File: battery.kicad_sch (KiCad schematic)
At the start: 25 parts

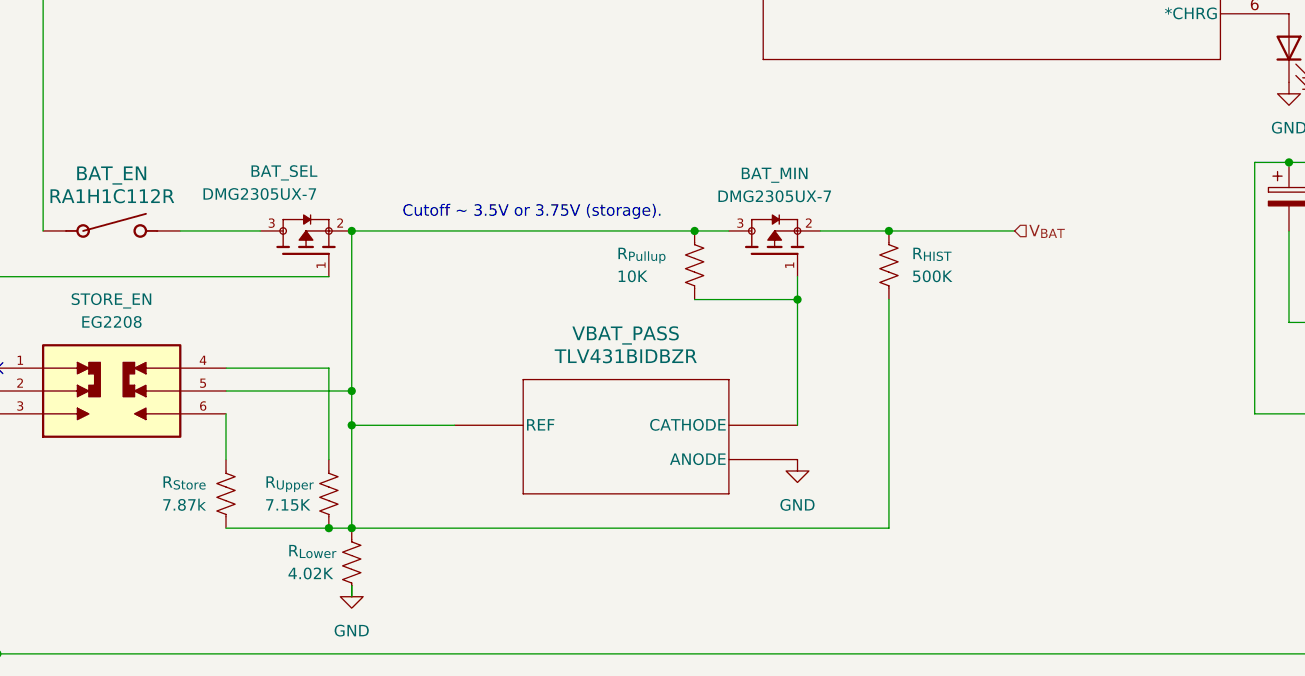
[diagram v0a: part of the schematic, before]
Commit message: Adjust battery resistor values
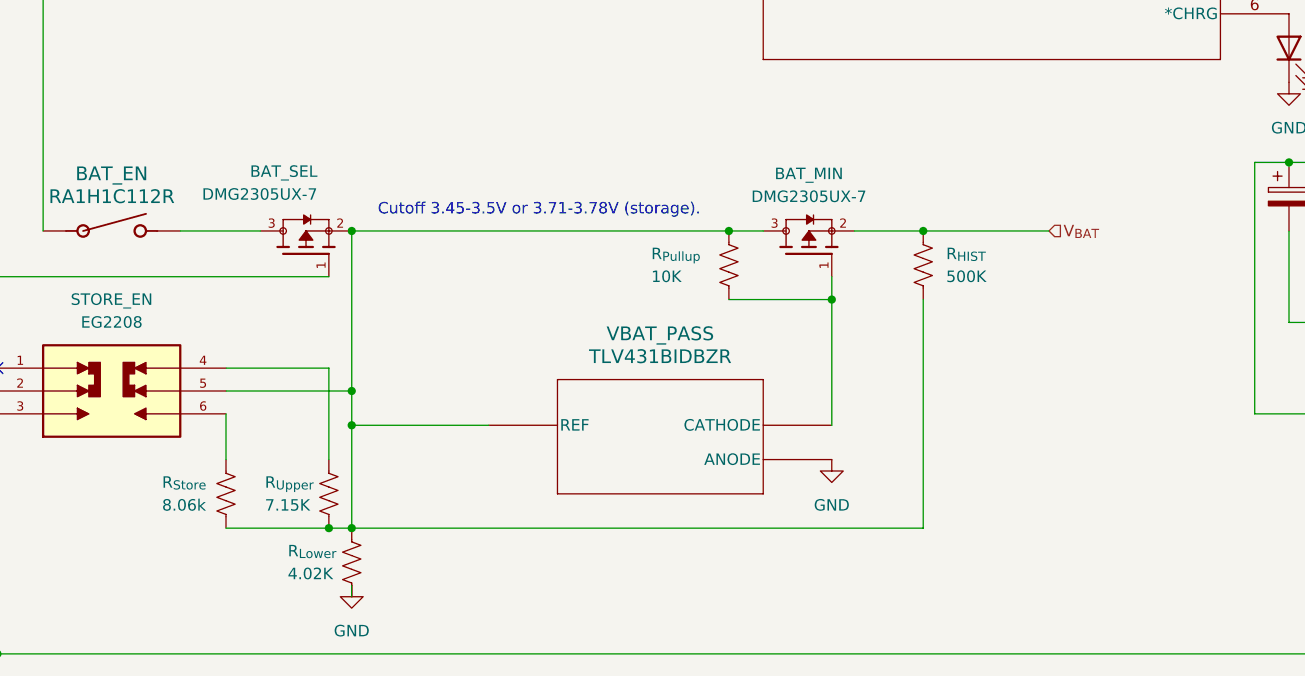
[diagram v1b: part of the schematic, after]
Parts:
- R_{Store}: value 7.87k -> 8.06k
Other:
- note added: "Cutoff 3.45-3.5V or 3.71-3.78V (storage)."
- note removed: "Cutoff ~ 3.5V or 3.75V (storage)."
- moved on the sheet: BAT_MIN, R_{HIST}, R_{Pullup}, VBAT_PASS
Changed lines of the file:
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@@
 		)
 	)
-	(text "Cutoff ~ 3.5V or 3.75V (storage).\n"
+	(text "Cutoff 3.45-3.5V or 3.71-3.78V (storage).\n"
 		(exclude_from_sim no)
-		(at 116.586 102.108 0)
+		(at 117.348 101.854 0)
 		(effects
 			(font
@@
 	)
 	(junction
-		(at 146.05 111.76)
+		(at 149.86 111.76)
 		(diameter 0)
 		(color 0 0 0 0)
@@
 	)
 	(junction
-		(at 134.62 104.14)
+		(at 138.43 104.14)
 		(diameter 0)
 		(color 0 0 0 0)
@@
 	)
 	(junction
-		(at 156.21 104.14)
+		(at 160.02 104.14)
 		(diameter 0)
 		(color 0 0 0 0)
@@
 	(wire
 		(pts
-			(xy 134.62 111.76) (xy 146.05 111.76)
+			(xy 138.43 111.76) (xy 149.86 111.76)
 		)
 		(stroke
@@
 	(wire
 		(pts
-			(xy 156.21 137.16) (xy 156.21 111.76)
+			(xy 160.02 137.16) (xy 160.02 111.76)
 		)
 		(stroke
@@
 	(wire
 		(pts
-			(xy 146.05 111.76) (xy 146.05 109.22)
+			(xy 149.86 111.76) (xy 149.86 109.22)
 		)
 		(stroke
@@
 	(wire
 		(pts
-			(xy 146.05 111.76) (xy 146.05 125.73)
+			(xy 149.86 111.76) (xy 149.86 125.73)
 		)
 		(stroke
@@
 	(wire
 		(pts
-			(xy 107.95 125.73) (xy 96.52 125.73)
+			(xy 111.76 125.73) (xy 96.52 125.73)
 		)
 		(stroke
@@
 	(wire
 		(pts
-			(xy 148.59 104.14) (xy 156.21 104.14)
+			(xy 152.4 104.14) (xy 160.02 104.14)
 		)
 		(stroke
@@
 	(wire
 		(pts
-			(xy 156.21 104.14) (xy 170.18 104.14)
+			(xy 160.02 104.14) (xy 173.99 104.14)
 		)
 		(stroke
@@
 	(wire
 		(pts
-			(xy 96.52 104.14) (xy 134.62 104.14)
+			(xy 96.52 104.14) (xy 138.43 104.14)
 		)
 		(stroke
@@
 	(wire
 		(pts
-			(xy 134.62 104.14) (xy 138.43 104.14)
+			(xy 138.43 104.14) (xy 142.24 104.14)
 		)
 		(stroke
@@
 	(wire
 		(pts
-			(xy 96.52 137.16) (xy 156.21 137.16)
+			(xy 96.52 137.16) (xy 160.02 137.16)
 		)
 		(stroke
@@
 	(hierarchical_label "V_{BAT}"
 		(shape input)
-		(at 170.18 104.14 0)
+		(at 173.99 104.14 0)
 		(effects
 			(font
@@
 	(symbol
 		(lib_id "DMG2305UX-7:DMG2305UX-7")
-		(at 143.51 106.68 90)
+		(at 147.32 106.68 90)
 		(unit 1)
 		(exclude_from_sim no)
@@
 		(fields_autoplaced yes)
 		(property "Reference" "BAT_MIN"
-			(at 143.51 97.79 90)
+			(at 147.32 97.79 90)
 			(effects
 				(font
@@
 		)
 		(property "Value" "DMG2305UX-7"
-			(at 143.51 100.33 90)
+			(at 147.32 100.33 90)
 			(effects
 				(font
@@
 		)
 		(property "Footprint" "DMG2305UX-7:SOT91P240X110-3N_DMG2305UX-7"
-			(at 143.51 106.68 0)
+			(at 147.32 106.68 0)
 			(effects
 				(font
@@
 		)
 		(property "Datasheet" ""
-			(at 143.51 106.68 0)
+			(at 147.32 106.68 0)
 			(effects
 				(font
@@
 		)
 		(property "Description" ""
-			(at 143.51 106.68 0)
+			(at 147.32 106.68 0)
 			(effects
 				(font
@@
 		)
 		(property "PARTREV" "09/2018"
-			(at 143.51 106.68 0)
+			(at 147.32 106.68 0)
 			(effects
 				(font
@@
 		)
 		(property "MANUFACTURER" "Diodes Inc."
-			(at 143.51 106.68 0)
+			(at 147.32 106.68 0)
 			(effects
 				(font
@@
 		)
 		(property "MAXIMUM_PACKAGE_HEIGHT" "1.1mm"
-			(at 143.51 106.68 0)
+			(at 147.32 106.68 0)
 			(effects
 				(font
@@
 		)
 		(property "STANDARD" "IPC-7351B"
-			(at 143.51 106.68 0)
+			(at 147.32 106.68 0)
 			(effects
 				(font
@@
 	(symbol
 		(lib_id "TLV431BIDBZR:TLV431BIDBZR")
-		(at 93.98 125.73 0)
+		(at 97.79 125.73 0)
 		(unit 1)
 		(exclude_from_sim no)
@@
 		(fields_autoplaced yes)
 		(property "Reference" "VBAT_PASS"
-			(at 127 115.57 0)
+			(at 130.81 115.57 0)
 			(effects
 				(font
@@
 		)
 		(property "Value" "TLV431BIDBZR"
-			(at 127 118.11 0)
+			(at 130.81 118.11 0)
 			(effects
 				(font
@@
 		)
 		(property "Footprint" "DBZ3"
-			(at 93.98 125.73 0)
+			(at 97.79 125.73 0)
 			(effects
 				(font
@@
 		)
 		(property "Datasheet" "https://www.ti.com/lit/gpn/tlv431b"
-			(at 93.98 125.73 0)
+			(at 97.79 125.73 0)
 			(effects
 				(font
@@
 		)
 		(property "Description" ""
-			(at 93.98 125.73 0)
+			(at 97.79 125.73 0)
 			(effects
 				(font
@@
 	(symbol
 		(lib_id "power:GND")
-		(at 146.05 129.54 0)
+		(at 149.86 129.54 0)
 		(unit 1)
 		(exclude_from_sim no)
@@
 		(fields_autoplaced yes)
 		(property "Reference" "#PWR019"
-			(at 146.05 135.89 0)
+			(at 149.86 135.89 0)
 			(effects
 				(font
@@
 		)
 		(property "Value" "GND"
-			(at 146.05 134.62 0)
+			(at 149.86 134.62 0)
 			(effects
 				(font
@@
 		)
 		(property "Footprint" ""
-			(at 146.05 129.54 0)
+			(at 149.86 129.54 0)
 			(effects
 				(font
@@
 		)
 		(property "Datasheet" ""
-			(at 146.05 129.54 0)
+			(at 149.86 129.54 0)
 			(effects
 				(font
@@
 		)
 		(property "Description" "Power symbol creates a global label with name \"GND\" , ground"
-			(at 146.05 129.54 0)
+			(at 149.86 129.54 0)
 			(effects
 				(font
@@
 	(symbol
 		(lib_id "Device:R_US")
-		(at 134.62 107.95 0)
+		(at 138.43 107.95 0)
 		(unit 1)
 		(exclude_from_sim no)
@@
 		(dnp no)
 		(property "Reference" "R_{Pullup}"
-			(at 125.984 106.68 0)
+			(at 129.794 106.68 0)
 			(effects
 				(font
@@
 		)
 		(property "Value" "10K"
-			(at 125.984 109.22 0)
+			(at 129.794 109.22 0)
 			(effects
 				(font
@@
 		)
 		(property "Footprint" ""
-			(at 135.636 108.204 90)
+			(at 139.446 108.204 90)
 			(effects
 				(font
@@
 		)
 		(property "Datasheet" "~"
-			(at 134.62 107.95 0)
+			(at 138.43 107.95 0)
 			(effects
 				(font
@@
 		)
 		(property "Description" "Resistor, US symbol"
-			(at 134.62 107.95 0)
+			(at 138.43 107.95 0)
 			(effects
 				(font
@@
 	(symbol
 		(lib_id "Device:R_US")
-		(at 156.21 107.95 0)
+		(at 160.02 107.95 0)
 		(unit 1)
 		(exclude_from_sim no)
@@
 		(fields_autoplaced yes)
 		(property "Reference" "R_{HIST}"
-			(at 158.75 106.6799 0)
+			(at 162.56 106.6799 0)
 			(effects
 				(font
@@
 		)
 		(property "Value" "500K"
-			(at 158.75 109.2199 0)
+			(at 162.56 109.2199 0)
 			(effects
 				(font
@@
 		)
 		(property "Footprint" ""
-			(at 157.226 108.204 90)
+			(at 161.036 108.204 90)
 			(effects
 				(font
@@
 		)
 		(property "Datasheet" "~"
-			(at 156.21 107.95 0)
+			(at 160.02 107.95 0)
 			(effects
 				(font
@@
 		)
 		(property "Description" "Resistor, US symbol"
-			(at 156.21 107.95 0)
+			(at 160.02 107.95 0)
 			(effects
 				(font
@@
 			)
 		)
-		(property "Value" "7.87k"
+		(property "Value" "8.06k"
 			(at 75.438 134.62 0)
 			(effects

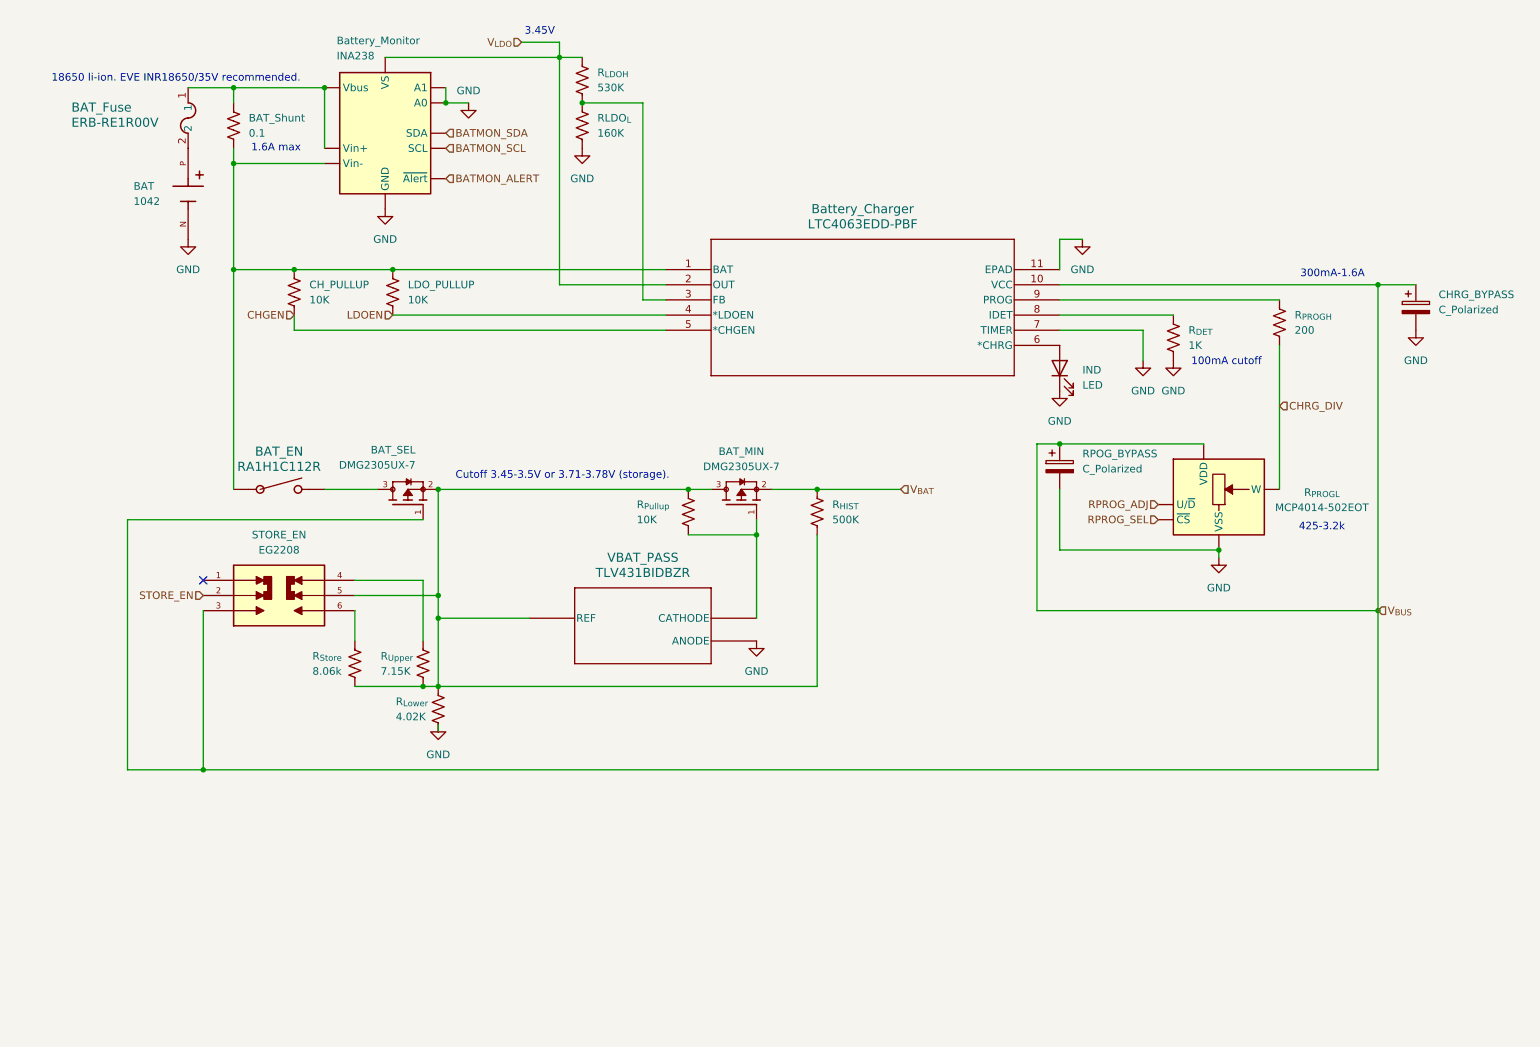
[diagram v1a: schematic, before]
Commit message: Rework battery entirely
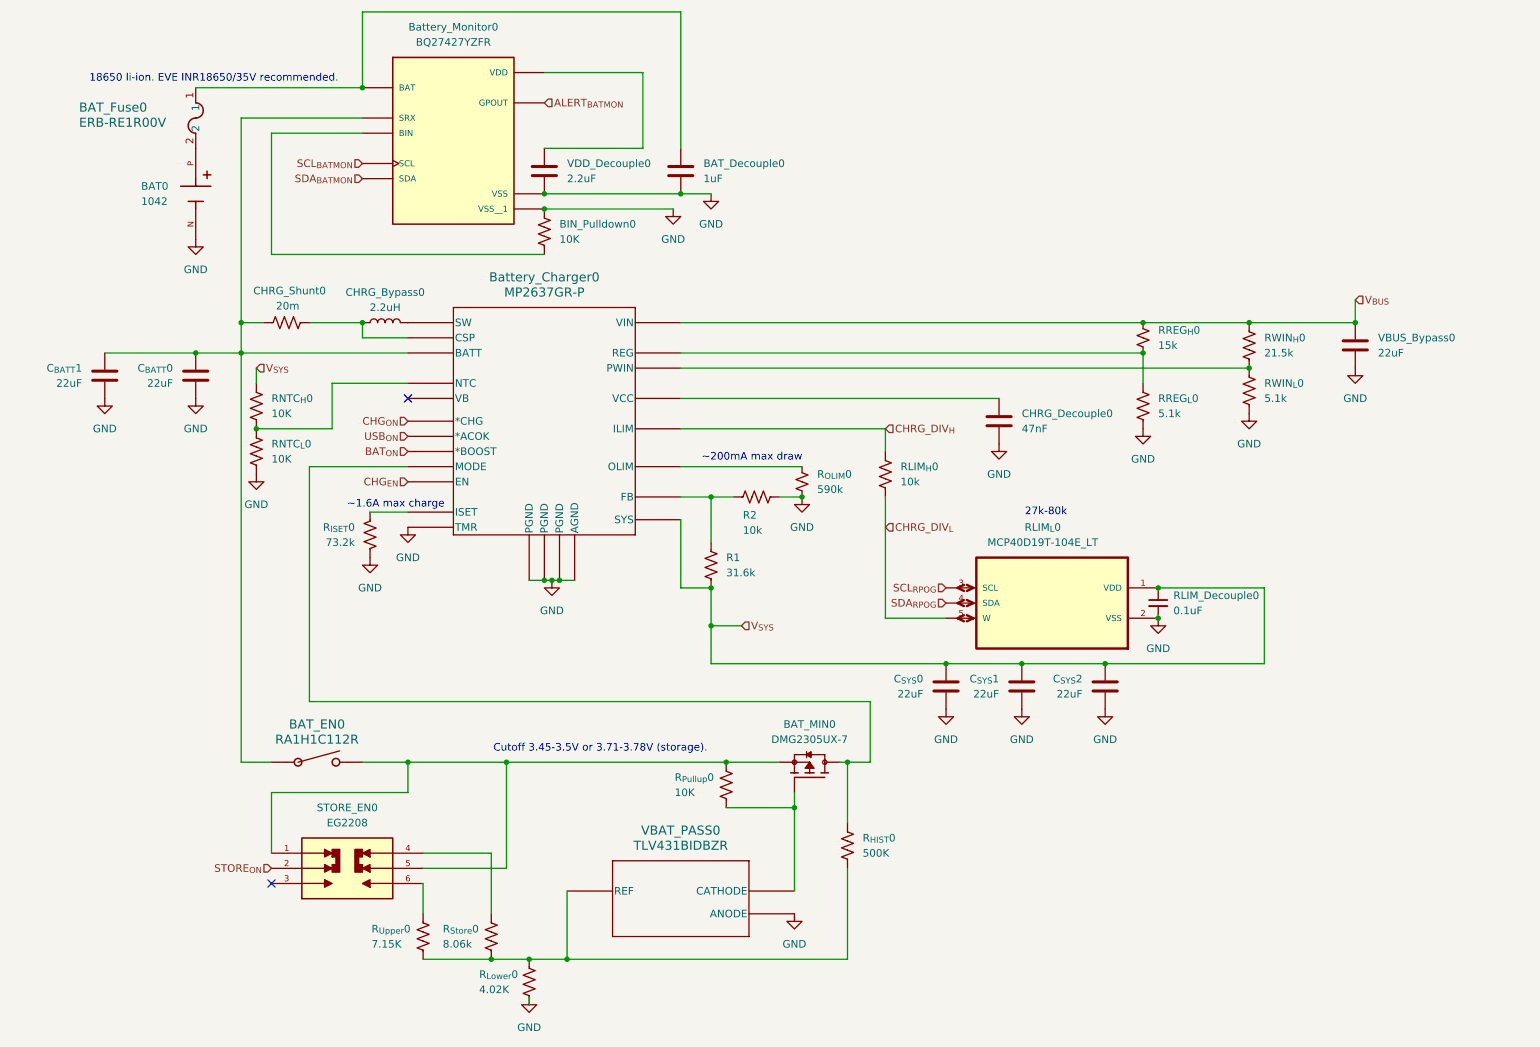
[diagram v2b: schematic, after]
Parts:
- removed BAT_SEL: DMG2305UX-7, DMG2305UX-7:SOT91P240X110-3N_DMG2305UX-7, symbol DMG2305UX-7:DMG2305UX-7
- removed BAT_Shunt: 0.1, symbol Device:R_US
- removed Battery_Charger: LTC4063EDD-PBF, DFN-10_DD_LIT, symbol LTC4063:LTC4063EDD-PBF
- removed Battery_Monitor: INA238, Package_SO:VSSOP-10_3x3mm_P0.5mm, symbol Sensor_Energy:INA238
- removed CHRG_BYPASS, RPOG_BYPASS: C_Polarized, symbol Device:C_Polarized
- removed CH_PULLUP, LDO_PULLUP: 10K, symbol Device:R_US
- removed IND: LED, symbol Device:LED
- removed RLDO_{L}: 160K, symbol Device:R_US
- removed R_{DET}: 1K, symbol Device:R_US
- removed R_{LDOH}: 530K, symbol Device:R_US
- removed R_{PROGH}: 200, symbol Device:R_US
- removed R_{PROGL}: MCP4014-502EOT, Package_TO_SOT_SMD:SOT-23-5, symbol Potentiometer_Digital:MCP4014-xxxxOT
- added BAT_Decouple0: 1uF, symbol Device:C
- added BIN_Pulldown0, RNTC_{H}0, RNTC_{L}0: 10K, symbol Device:R_US
- added Battery_Charger0: MP2637GR-P, QFN-24_MP2637_MNP, symbol MP2637GR-P:MP2637GR-P
- added Battery_Monitor0: BQ27427YZFR, BQ27427YZFR:IC_BQ27427YZFR, symbol BQ27427YZFR:BQ27427YZFR
- added CHRG_Bypass0: 2.2uH, symbol Device:L
- added CHRG_Decouple0: 47nF, symbol Device:C
- added CHRG_Shunt0: 20m, symbol Device:R_US
- added C_{BATT}0, C_{BATT}1, C_{SYS}0, C_{SYS}1, C_{SYS}2, VBUS_Bypass0: 22uF, symbol Device:C
- added R1: 31.6k, symbol Device:R_US
- added R2, RLIM_{H}0: 10k, symbol Device:R_US
- added RLIM_Decouple0: 0.1uF, symbol Device:C_Small
- added RLIM_{L}0: MCP40D19T-104E_LT, MCP40D19T-104E_LT:SOT65P210X110-5N, symbol MCP40D19T-104E_LT:MCP40D19T-104E_LT
- added RREG_{H}0: 15k, symbol Device:R_Small_US
- added RREG_{L}0, RWIN_{L}0: 5.1k, symbol Device:R_US
- added RWIN_{H}0: 21.5k, symbol Device:R_US
- added R_{ISET}0: 73.2k, symbol Device:R_US
- added R_{OLIM}0: 590k, symbol Device:R_Small_US
- added VDD_Decouple0: 2.2uF, symbol Device:C
- renumbered BAT to BAT0, BAT_EN to BAT_EN0, BAT_Fuse to BAT_Fuse0, BAT_MIN to BAT_MIN0, R_{HIST} to R_{HIST}0, R_{Lower} to R_{Lower}0, R_{Pullup} to R_{Pullup}0, R_{Store} to R_{Store}0, R_{Upper} to R_{Upper}0, STORE_EN to STORE_EN0, VBAT_PASS to VBAT_PASS0
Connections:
- net GND: now also BAT_Decouple0.2, BIN_Pulldown0.1, Battery_Charger0.1 (PGND), Battery_Charger0.13 (TMR), Battery_Charger0.23 (PGND), Battery_Charger0.24 (PGND), Battery_Charger0.6 (AGND), Battery_Monitor0.B2 (VSS), Battery_Monitor0.C1 (VSS__1), CHRG_Decouple0.2, C_{BATT}0.2, C_{BATT}1.2, C_{SYS}0.2, C_{SYS}1.2, C_{SYS}2.2, R2.1, RLIM_Decouple0.2, RLIM_{L}0.2 (VSS), RNTC_{L}0.2, RREG_{L}0.2, RWIN_{L}0.2, R_{ISET}0.2, R_{OLIM}0.2, VBUS_Bypass0.2, VDD_Decouple0.2
- net V_{BUS}: now also Battery_Charger0.20 (VIN), RREG_{H}0.1, RWIN_{H}0.1, VBUS_Bypass0.1; no longer STORE_EN0.3
- net at R_{HIST}0.2, R_{Lower}0.1, R_{Store}0.2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: no longer BAT_MIN0.3, R_{Pullup}0.1, STORE_EN0.5
- net at BAT_EN0.2: now also BAT_MIN0.2, R_{Pullup}0.1, STORE_EN0.1, STORE_EN0.5
- net at BAT_EN0.1: now also Battery_Charger0.5 (BATT), Battery_Monitor0.C2 (SRX), CHRG_Shunt0.1, C_{BATT}0.1, C_{BATT}1.1
- net at BAT_Fuse0.1: now also BAT_Decouple0.1, Battery_Monitor0.C3 (BAT)
- net at R_{Upper}0.1: now also STORE_EN0.6; no longer STORE_EN0.4
- net at R_{Store}0.1: now also STORE_EN0.4; no longer STORE_EN0.6
- net STORE_EN renamed STORE_{ON}
- net V_{BAT}: no longer names the net of R_{HIST}0.1
- net V_{BAT}: now also BAT_MIN0.3, Battery_Charger0.19 (MODE); no longer BAT_MIN0.2
- new net: Battery_Charger0.12 (REG), RREG_{H}0.2, RREG_{L}0.1
- new net: BIN_Pulldown0.2, Battery_Monitor0.B1 (BIN)
- new net: Battery_Monitor0.B3 (VDD), VDD_Decouple0.1
- new net: Battery_Charger0.9 (NTC), RNTC_{H}0.2, RNTC_{L}0.1
- new net: Battery_Charger0.14 (PWIN), RWIN_{H}0.2, RWIN_{L}0.1
- new net: Battery_Charger0.4 (CSP), CHRG_Bypass0.1, CHRG_Shunt0.2
- new net: Battery_Charger0.16 (VCC), CHRG_Decouple0.1
- new net: Battery_Charger0.10 (FB), R1.1, R2.2
- new net: Battery_Charger0.22 (SW), CHRG_Bypass0.2
- new net: Battery_Charger0.7 (OLIM), R_{OLIM}0.1
- new net: Battery_Charger0.8 (ISET), R_{ISET}0.1
- new net ALERT_{BATMON}: Battery_Monitor0.A1 (GPOUT)
- new net BAT_{ON}: Battery_Charger0.3 (*BOOST)
- new net CHG_{EN}: Battery_Charger0.18 (EN)
- new net CHG_{ON}: Battery_Charger0.2 (*CHG)
- new net CHRG_DIV_{H}: Battery_Charger0.15 (ILIM), RLIM_{H}0.1
- new net CHRG_DIV_{L}: RLIM_{H}0.2, RLIM_{L}0.5 (W)
- new net SCL_{BATMON}: Battery_Monitor0.A3 (SCL)
- new net SCL_{RPOG}: RLIM_{L}0.3 (SCL)
- new net SDA_{BATMON}: Battery_Monitor0.A2 (SDA)
- new net SDA_{RPOG}: RLIM_{L}0.4 (SDA)
- new net USB_{ON}: Battery_Charger0.11 (*ACOK)
- new net V_{SYS}: Battery_Charger0.21 (SYS), C_{SYS}0.1, C_{SYS}1.1, C_{SYS}2.1, R1.2, RLIM_Decouple0.1, RLIM_{L}0.1 (VDD), RNTC_{H}0.1
- no-connect marks 1 -> 2
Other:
- note added: "27k-80k"
- note added: "~1.6A max charge"
- note added: "~200mA max draw"
- note removed: "1.6A max"
- note removed: "100mA cutoff"
- note removed: "3.45V"
- note removed: "300mA-1.6A"
- note removed: "425-3.2k"
- moved on the sheet: BAT0, BAT_EN0, BAT_Fuse0, R_{HIST}0, R_{Lower}0, R_{Pullup}0, R_{Store}0, R_{Upper}0, STORE_EN0, VBAT_PASS0
